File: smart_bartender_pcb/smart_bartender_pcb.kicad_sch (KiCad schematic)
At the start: 45 parts, among them J1 Screw_Terminal_01x02, U1 AMS1117-5.0, U2 ULN2803A

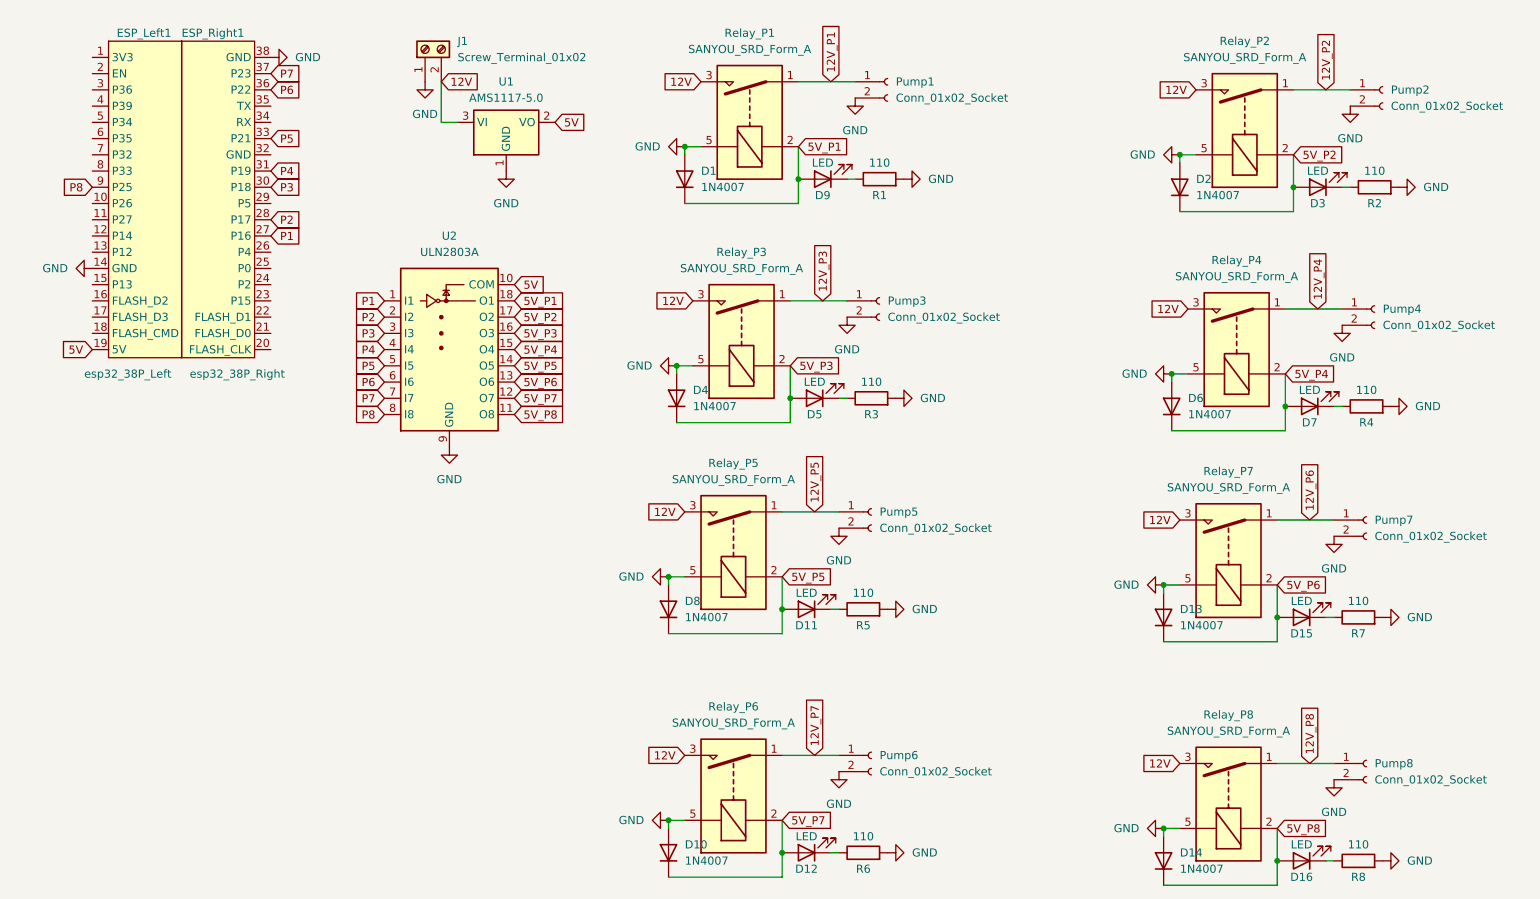
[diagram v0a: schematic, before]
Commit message: started pcb layout
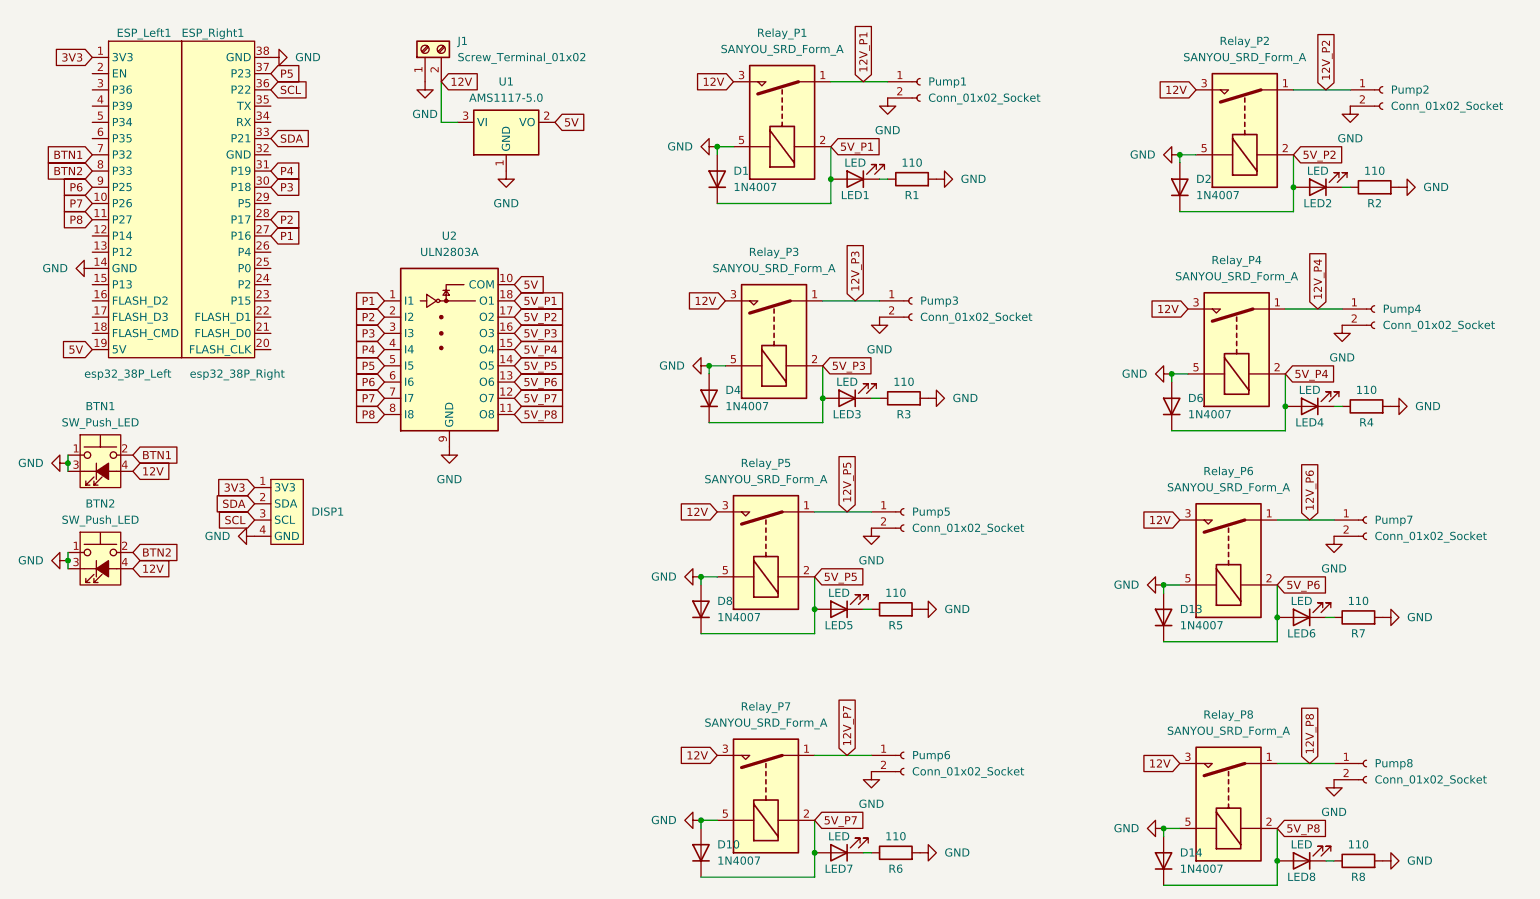
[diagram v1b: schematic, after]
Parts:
- added BTN1, BTN2: SW_Push_LED, Connector_PinHeader_2.54mm:PinHeader_1x04_P2.54mm_Vertical, symbol Switch:SW_Push_LED
- added DISP1: ~, Connector_PinSocket_2.54mm:PinSocket_1x04_P2.54mm_Horizontal, symbol custom:I2C_Pads
- renumbered D9 to LED1, D3 to LED2, D5 to LED3, D7 to LED4, D11 to LED5, D15 to LED6, D12 to LED7, D16 to LED8, Relay_P7 to Relay_P6, Relay_P6 to Relay_P7
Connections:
- net 12V: now also BTN1.4 (A), BTN2.4 (A)
- net GND: now also BTN1.1, BTN1.3 (K), BTN2.1, BTN2.3 (K), DISP1.4 (GND)
- net P5: now also ESP_Right1.37 (P23); no longer ESP_Right1.33 (P21)
- net P6: now also ESP_Left1.9 (P25); no longer ESP_Right1.36 (P22)
- net P7: now also ESP_Left1.10 (P26); no longer ESP_Right1.37 (P23)
- net P8: now also ESP_Left1.11 (P27); no longer ESP_Left1.9 (P25)
- net 3V3: now reaches ESP_Left1.1 (3V3)
- net 3V3: now also DISP1.1 (3V3)
- net BTN1: now reaches ESP_Left1.7 (P32)
- net BTN1: now also BTN1.2
- net BTN2: now reaches ESP_Left1.8 (P33)
- net BTN2: now also BTN2.2
- new net SCL: DISP1.3 (SCL), ESP_Right1.36 (P22)
- new net SDA: DISP1.2 (SDA), ESP_Right1.33 (P21)
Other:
- moved on the sheet: D1, D10, D4, D8, LED1, LED3, LED5, LED7, Pump1, Pump3, Pump5, Pump6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
